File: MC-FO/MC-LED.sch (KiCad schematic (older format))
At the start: 10 parts, among them U181 TPS3703A5330DSER, U182 74ACT08SCX, U183 TPS3703A5500DSER

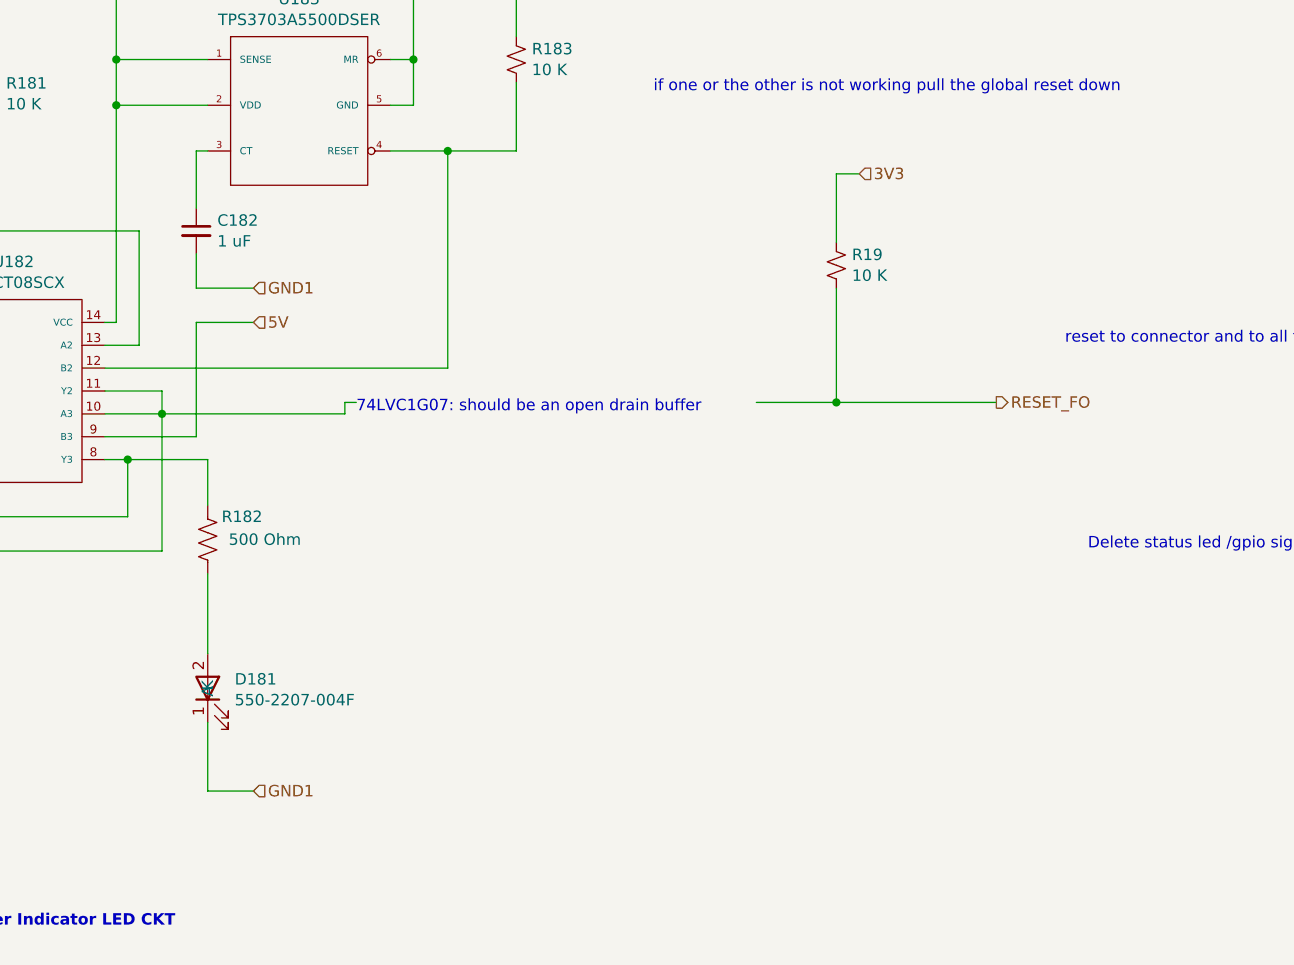
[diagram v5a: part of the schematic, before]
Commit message: add connector, reset implementation
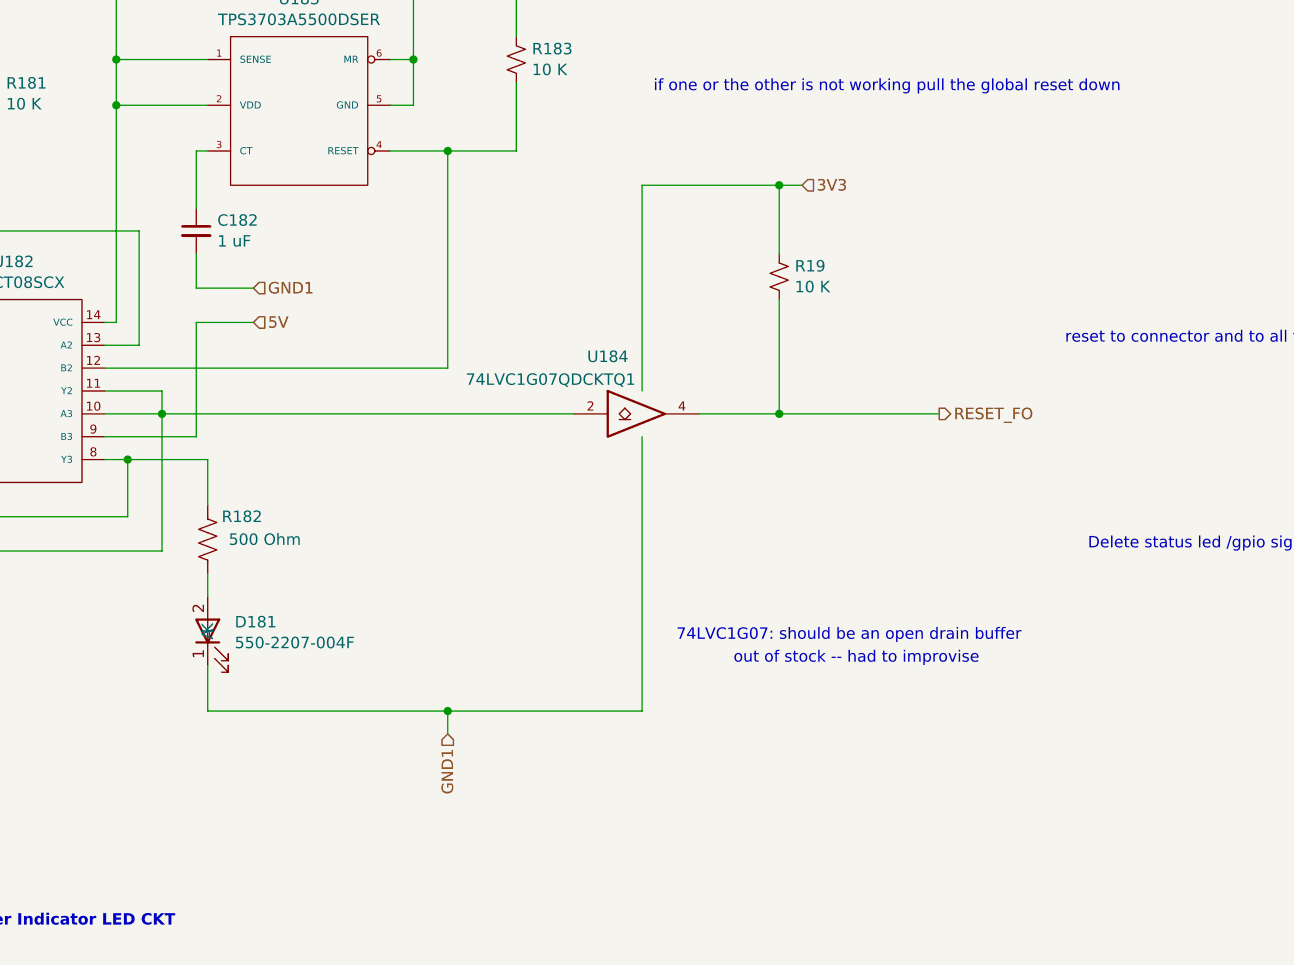
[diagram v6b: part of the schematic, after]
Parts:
- added U184: 74LVC1G07QDCKTQ1, Package_TO_SOT_SMD:SOT-353_SC-70-5, symbol Existing_IC_Models:74LVC1G07QDCKTQ1
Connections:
- net RESET_FO: now also U184.4
- net at U182.10 (A3), U182.11 (Y2), U182.2 (B0)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: now also U184.2
- net 3V3 renamed VCC
- net VCC: now also U184.5 (VCC)
- net GND1 renamed GND
- net GND: now also U184.3 (GND)
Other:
- note added: "out of stock -- had to improvise\n"
- moved on the sheet: D181, R19
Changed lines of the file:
@@
 	-1   0    0    1
 $EndComp
-Wire Wire Line
-	3850 5450 3850 5750
-Wire Wire Line
-	3850 5750 4050 5750
-Text HLabel 4050 5750 2    50   Input ~ 0
+Text HLabel 4900 5500 3    50   Input ~ 0
 GND1
 Text HLabel 3400 2150 0    50   Input ~ 0
@@
 Wire Wire Line
 	3850 4300 3850 4500
-Wire Wire Line
-	3850 4800 3850 5150
 Text HLabel 2950 2150 2    50   Input ~ 0
 3V3
@@
 L Existing_IC_Models:550-2207-004F D?
 U 1 1 61797676
-P 3750 5300
+P 3750 5050
 AR Path="/61797676" Ref="D?"  Part="1"
 AR Path="/6175812E/61797676" Ref="D181"  Part="1"
-F 0 "D181" V 3789 5082 50  0000 R CNN
-F 1 "550-2207-004F" V 3698 5082 50  0000 R CNN
-F 2 "Footprints_MC-FO:550-2207-004F" H 3750 5400 50  0001 C CNN
-F 3 "" H 3750 5400 50  0001 C CNN
-	1    3750 5300
+F 0 "D181" V 3789 4832 50  0000 R CNN
+F 1 "550-2207-004F" V 3698 4832 50  0000 R CNN
+F 2 "Footprints_MC-FO:550-2207-004F" H 3750 5150 50  0001 C CNN
+F 3 "" H 3750 5150 50  0001 C CNN
+	1    3750 5050
 	0    -1   -1   0
 $EndComp
@@
 Text Notes 5800 2700 0    50   ~ 0
 if one or the other is not working pull the global reset down
-Text Notes 4500 4100 0    50   ~ 0
+Text Notes 5900 5100 0    50   ~ 0
 74LVC1G07: should be an open drain buffer\n
 Wire Wire Line
-	3650 4100 4450 4100
-Wire Wire Line
-	4450 4100 4450 4050
-Wire Wire Line
-	4450 4050 4500 4050
-Wire Wire Line
-	6250 4050 6600 4050
+	6000 4100 6350 4100
 Text Notes 7600 3800 0    50   ~ 0
 reset to connector and to all transcievers
-Connection ~ 6600 4050
-Wire Wire Line
-	6600 4050 7300 4050
+Connection ~ 6350 4100
+Wire Wire Line
+	6350 4100 7050 4100
 $Comp
 L Device:R_Small_US R19
 U 1 1 6182FD38
-P 6600 3450
-F 0 "R19" H 6668 3496 50  0000 L CNN
-F 1 "10 K" H 6668 3405 50  0000 L CNN
-F 2 "Resistor_SMD:R_0603_1608Metric" H 6600 3450 50  0001 C CNN
-F 3 "~" H 6600 3450 50  0001 C CNN
-	1    6600 3450
-	1    0    0    -1
-$EndComp
-Text HLabel 6700 3050 2    50   Input ~ 0
+P 6350 3500
+F 0 "R19" H 6418 3546 50  0000 L CNN
+F 1 "10 K" H 6418 3455 50  0000 L CNN
+F 2 "Resistor_SMD:R_0603_1608Metric" H 6350 3500 50  0001 C CNN
+F 3 "~" H 6350 3500 50  0001 C CNN
+	1    6350 3500
+	1    0    0    -1
+$EndComp
+Text HLabel 6450 3100 2    50   Input ~ 0
 3V3
 Wire Wire Line
-	6700 3050 6600 3050
-Wire Wire Line
-	6600 3050 6600 3350
-Wire Wire Line
-	6600 3550 6600 4050
-Text HLabel 7300 4050 2    50   Output ~ 0
+	6450 3100 6350 3100
+Wire Wire Line
+	6350 3100 6350 3400
+Wire Wire Line
+	6350 3600 6350 4100
+Text HLabel 7050 4100 2    50   Output ~ 0
 RESET_FO
+$Comp
+L Existing_IC_Models:74LVC1G07QDCKTQ1 U184
+U 1 1 617E8424
+P 5750 4100
+F 0 "U184" H 5600 4350 50  0000 C CNN
+F 1 "74LVC1G07QDCKTQ1" H 5350 4250 50  0000 C CNN
+F 2 "Package_TO_SOT_SMD:SOT-353_SC-70-5" H 5750 4100 50  0001 C CNN
+F 3 "http://www.ti.com/lit/sg/scyt129e/scyt129e.pdf" H 5750 4100 50  0001 C CNN
+	1    5750 4100
+	1    0    0    -1
+$EndComp
+Wire Wire Line
+	5750 4000 5750 3100
+Wire Wire Line
+	5750 3100 6350 3100
+Connection ~ 6350 3100
+Wire Wire Line
+	5750 5400 4900 5400
+Wire Wire Line
+	4900 5400 4900 5500
+Wire Wire Line
+	5750 4200 5750 5400
+Wire Wire Line
+	3850 4800 3850 4900
+Wire Wire Line
+	3850 5200 3850 5400
+Wire Wire Line
+	3850 5400 4900 5400
+Connection ~ 4900 5400
+Wire Wire Line
+	3650 4100 5450 4100
+Text Notes 6150 5200 0    50   ~ 0
+out of stock -- had to improvise\n
 $EndSCHEMATC

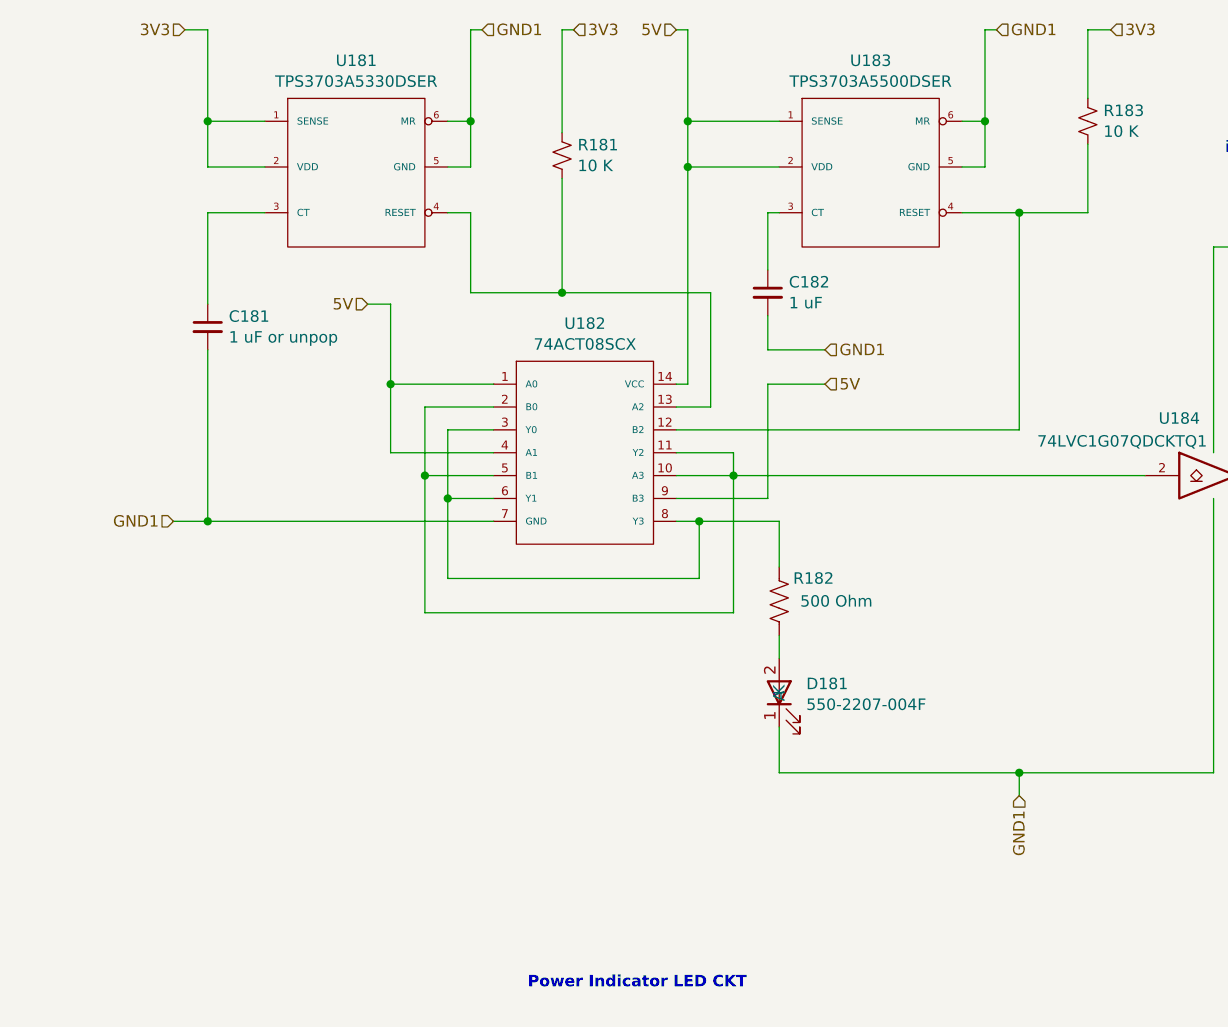
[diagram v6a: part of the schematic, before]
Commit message: changed status1 to output of detector
reassigned footprint of 550 LED
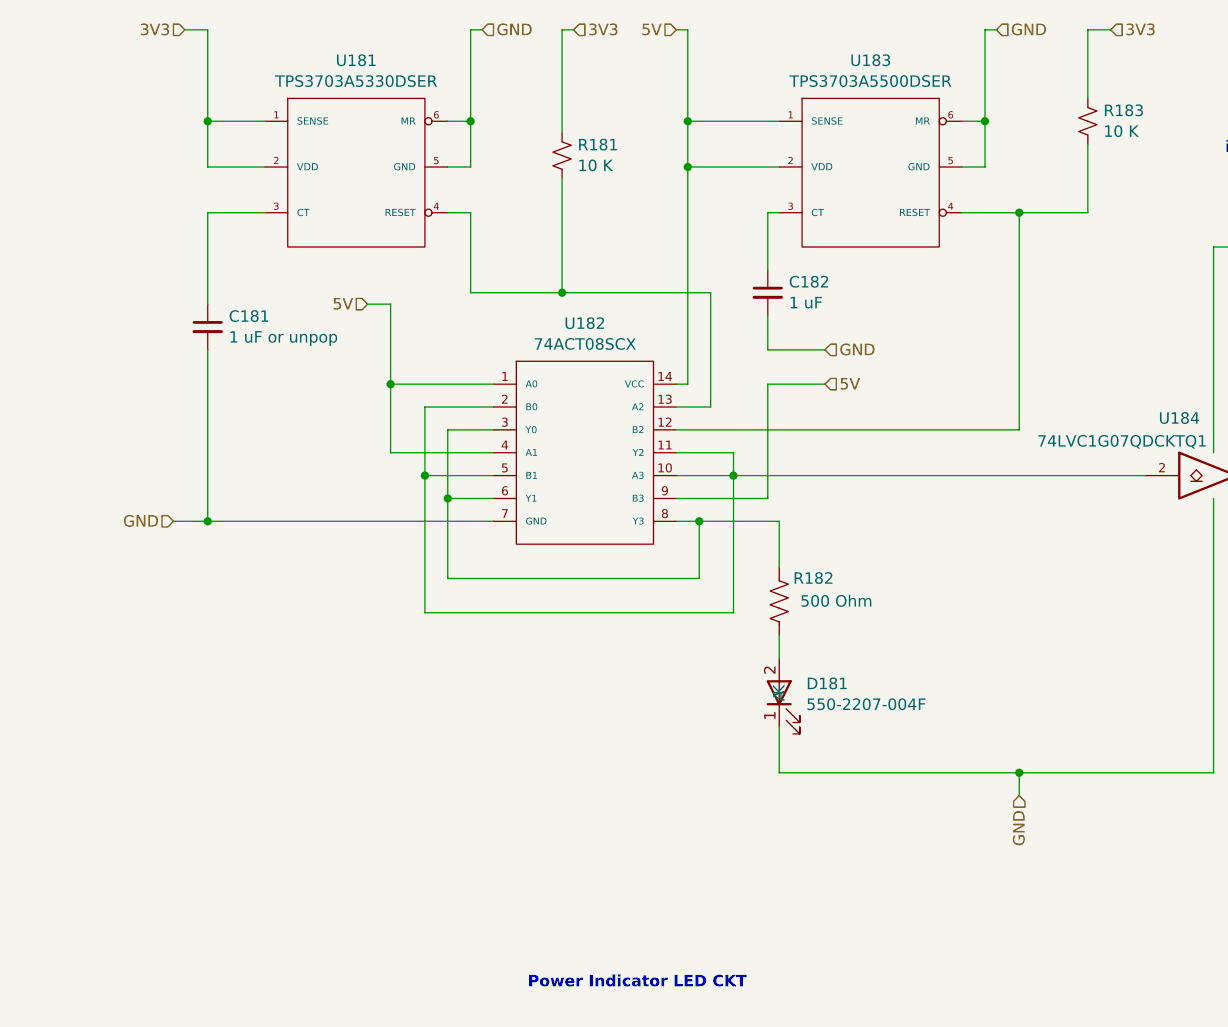
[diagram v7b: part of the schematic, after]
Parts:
- D181: footprint Footprints_MC-FO:550-2207-004F -> Footprints_MC-FO:5502207004F
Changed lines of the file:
@@
 $EndComp
 Text HLabel 4900 5500 3    50   Input ~ 0
-GND1
+GND
 Text HLabel 3400 2150 0    50   Input ~ 0
 5V
@@
 Connection ~ 1350 2550
 Text HLabel 2550 2150 2    50   Input ~ 0
-GND1
+GND
 Text HLabel 4800 2150 2    50   Input ~ 0
-GND1
+GND
 Wire Wire Line
 	3450 3700 3400 3700
@@
 	1350 2950 1350 3350
 Text HLabel 1200 4300 0    50   Input ~ 0
-GND1
+GND
 Wire Wire Line
 	2600 4300 1350 4300
@@
 Connection ~ 1350 4300
 Text HLabel 4050 3550 2    50   Input ~ 0
-GND1
+GND
 Wire Wire Line
 	3450 2150 3450 2550
@@
 F 0 "D181" V 3789 4832 50  0000 R CNN
 F 1 "550-2207-004F" V 3698 4832 50  0000 R CNN
-F 2 "Footprints_MC-FO:550-2207-004F" H 3750 5150 50  0001 C CNN
+F 2 "Footprints_MC-FO:5502207004F" H 3750 5150 50  0001 C CNN
 F 3 "" H 3750 5150 50  0001 C CNN
 	1    3750 5050

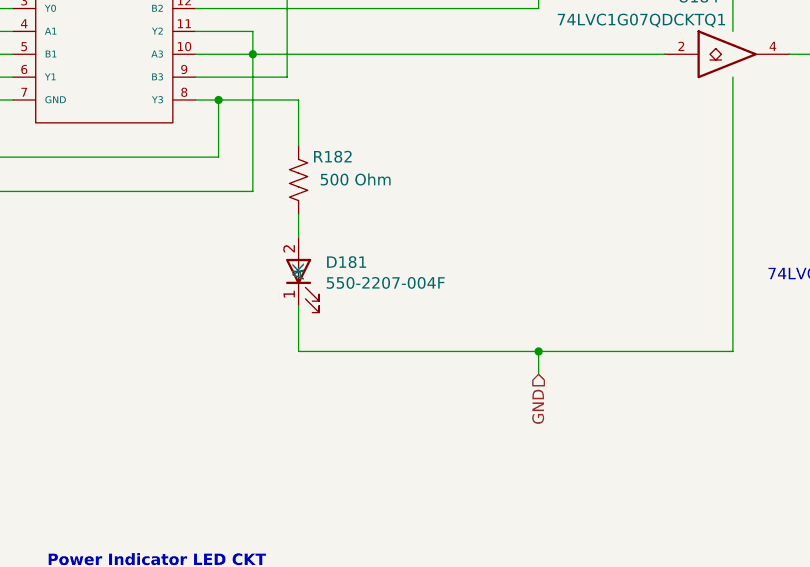
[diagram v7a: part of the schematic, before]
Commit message: Update LED, Transc. Footprint, layout
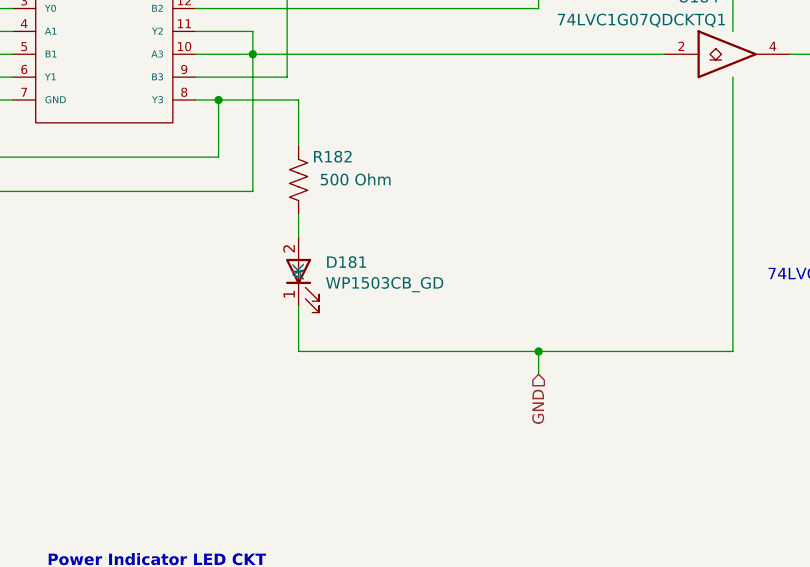
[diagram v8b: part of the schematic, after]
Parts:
- removed D181: 550-2207-004F, Footprints_MC-FO:5502207004F, symbol Existing_IC_Models:550-2207-004F
- added D181: WP1503CB_GD, Footprints_MC-FO:WP1503CBGD, symbol Existing_IC_Models:WP1503CB_GD
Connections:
- net GND: now also D181.1 (K)
- net at R182.1: now also D181.2 (A)
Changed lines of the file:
@@
 Wire Wire Line
 	3800 3550 4050 3550
-$Comp
-L Existing_IC_Models:550-2207-004F D?
-U 1 1 61797676
-P 3750 5050
-AR Path="/61797676" Ref="D?"  Part="1"
-AR Path="/6175812E/61797676" Ref="D181"  Part="1"
-F 0 "D181" V 3789 4832 50  0000 R CNN
-F 1 "550-2207-004F" V 3698 4832 50  0000 R CNN
-F 2 "Footprints_MC-FO:5502207004F" H 3750 5150 50  0001 C CNN
-F 3 "" H 3750 5150 50  0001 C CNN
-	1    3750 5050
-	0    -1   -1   0
-$EndComp
 Wire Wire Line
 	4750 2550 4650 2550
@@
 Text Notes 6150 5200 0    50   ~ 0
 out of stock -- had to improvise\n
+$Comp
+L Existing_IC_Models:WP1503CB_GD D181
+U 1 1 6185A99A
+P 3750 5050
+F 0 "D181" V 3789 4832 50  0000 R CNN
+F 1 "WP1503CB_GD" V 3698 4832 50  0000 R CNN
+F 2 "Footprints_MC-FO:WP1503CBGD" H 3750 5150 50  0001 C CNN
+F 3 "" H 3750 5150 50  0001 C CNN
+	1    3750 5050
+	0    -1   -1   0
+$EndComp
 $EndSCHEMATC
